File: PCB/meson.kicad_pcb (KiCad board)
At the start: 2 copper layers, 134.6 x 78.7 mm, 58 parts, among them K1 KEYSW, K10 KEYSW, K11 KEYSW, K12 KEYSW, K13 KEYSW, K14 KEYSW, K15 KEYSW, K16 KEYSW, K17 KEYSW, K18 KEYSW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

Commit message: wew
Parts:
- removed H1, H2: MountingHole, MountingHole:MountingHole_5.3mm_M5
- added REF**: MountingHole_3.2mm_M3, MountingHole:MountingHole_3.2mm_M3, F.Cu at (219.1, 104.8)
- added REF**: MountingHole_3.2mm_M3, MountingHole:MountingHole_3.2mm_M3, F.Cu at (200.0, 85.7)
- added REF**: MountingHole_3.2mm_M3, MountingHole:MountingHole_3.2mm_M3, F.Cu at (161.9, 85.7)
- added REF**: MountingHole_3.2mm_M3, MountingHole:MountingHole_3.2mm_M3, F.Cu at (200.0, 66.7)
- added REF**: MountingHole_3.2mm_M3, MountingHole:MountingHole_3.2mm_M3, F.Cu at (161.9, 66.7)
- moved D22 5.71 mm to (211.5, 105.2)
- moved D23 2.54 mm to (223.5, 105.2)
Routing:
- net /row3: track 80.6 -> 88.4 mm
- net /row2: track 169.8 -> 171.0 mm
- net /col1: track 124.8 -> 125.7 mm
- net Net-(D22-Pad2): track 19.9 -> 20.7 mm
- net Net-(D23-Pad2): track 4.24 -> 4.91 mm
- net /col2: track 106.4 -> 107.0 mm

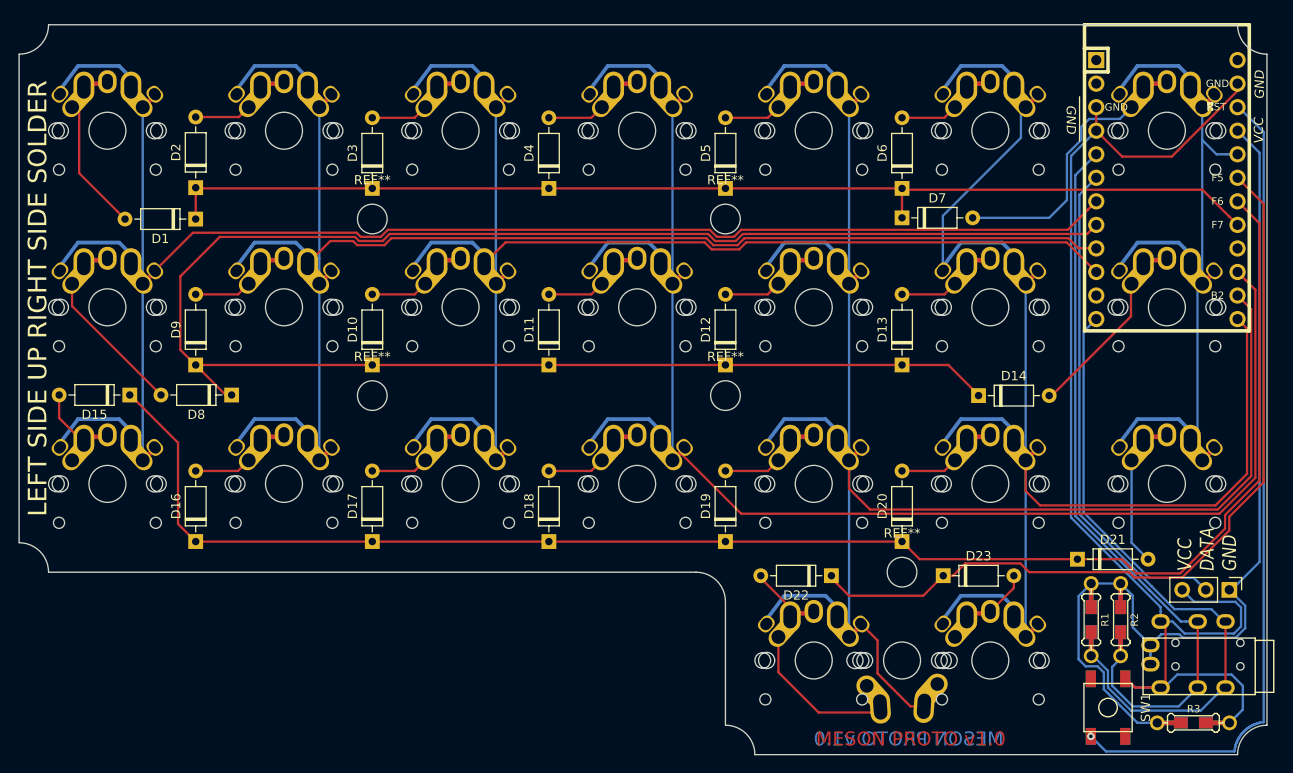
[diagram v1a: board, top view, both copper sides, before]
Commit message: "M3 mounting holes for pcb mounting+fixing big mistakes"
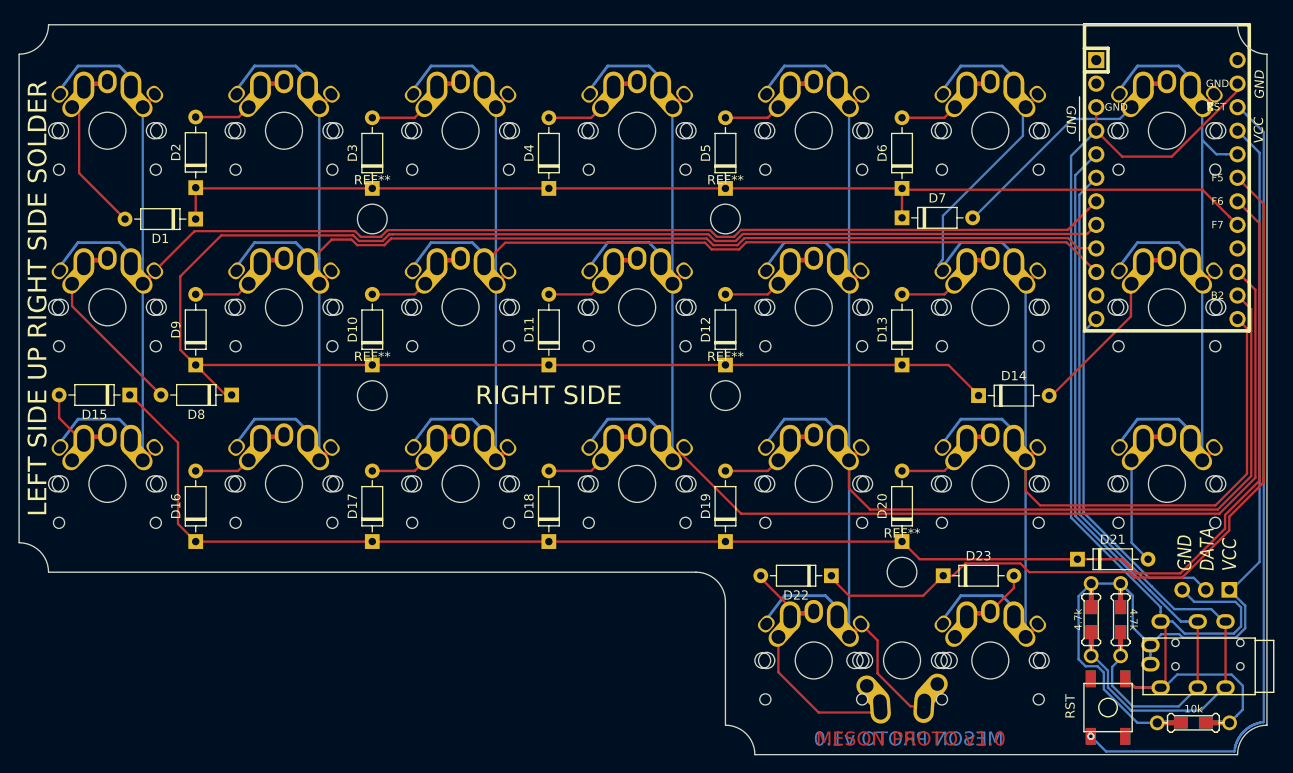
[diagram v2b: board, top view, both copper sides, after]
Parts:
- renumbered R3 to 10k, SW2 to RST, SW1 to RST
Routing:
- net Net-(D7-Pad2): track 26.9 -> 23.2 mm
- net /col6: track 40.9 -> 42.5 mm
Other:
- board text added: "4.7k"
- board text added: "GND DATA VCC"
- board text added: "LEFT SIDE"
- board text added: "RIGHT SIDE"
- board text removed: "VCC DATA GND"

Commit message: cleaning
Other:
- board text added: "LEFT SIDE?"
- board text removed: "LEFT SIDE"

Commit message: moving towards production
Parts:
- removed 10k: 10k, Keebio-Parts:Resistor-Hybrid
- added G***: LOGO, silks:pi, B.Cu at (143.0, 61.1)
- added G***: LOGO, silks:gluon, B.Cu at (166.3, 80.2)
- added G***: LOGO, silks:pi, B.Cu at (143.1, 80.5)
- added G***: LOGO, silks:pi, B.Cu at (143.2, 99.4)
- added G***: LOGO, silks:gluon, F.Cu at (199.9, 80.7)
- added G***: LOGO, silks:pi, F.Cu at (223.2, 61.6)
- added G***: LOGO, silks:pi, F.Cu at (223.1, 81.0)
- added G***: LOGO, silks:pi, F.Cu at (223.0, 99.9)
- added R3: 10k, Keebio-Parts:Resistor-Hybrid, F.Cu at (250.5, 121.0)
- moved REF** 38.1 mm to (238.1, 85.7)
- moved RGB1 0.25 mm to (254.4, 106.9)
- renumbered RST to SW1, RST to SW2
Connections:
- SW1 pad 3: (no net) -> Net-(SW1-Pad3)
- SW1 pad 4: (no net) -> Net-(SW1-Pad4)
- SW2 pad 1: (no net) -> Net-(SW2-Pad1)
- SW2 pad 2: (no net) -> Net-(SW2-Pad2)
- U1 pad 1: (no net) -> Net-(U1-Pad1)
- U1 pad 11: (no net) -> Net-(U1-Pad11)
- U1 pad 16: (no net) -> /row2
- U1 pad 17: /row0 -> /row3
- U1 pad 18: /row2 -> Net-(U1-Pad18)
- U1 pad 19: /row3 -> /row0
- U1 pad 2: (no net) -> Net-(U1-Pad2)
- U1 pad 24: (no net) -> Net-(U1-Pad24)
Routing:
- net GND: track 129.3 -> 111.3 mm
- net VCC: track 102.5 -> 87.1 mm
- net /row1: track 203.6 -> 198.2 mm
- net /row2: track 171.0 -> 166.0 mm
- net /row3: track 88.4 -> 83.8 mm
- net SCL: track 79.3 -> 81.5 mm
- net SDA: track 85.0 -> 87.0 mm
- net Net-(SW1-Pad2): track 88.6 -> 86.8 mm
- net LED: track 38.1 -> 39.3 mm
- net /col0: track 145.2 -> 143.9 mm
- net /row0: track 120.2 -> 119.2 mm
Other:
- outline, holes or cut-outs redrawn
- board text added: "+"
- board text added: "-"
- board text added: "K"
- board text added: "MESON v1.0"
- board text added: "W"
- board text added: "g"
- board text added: "s"
- board text added: "u"
- board text removed: "F.Cu aesthetic trace"
- board text removed: "LEFT SIDE UP RIGHT SIDE SOLDER"
- board text removed: "LEFT SIDE?"
- board text removed: "MESON PROTO v1.0"
- board text removed: "RIGHT SIDE"
- board text removed: "RIGHT SIDE UP LEFT SIDE SOLDER"
